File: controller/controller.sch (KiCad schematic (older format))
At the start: 23 parts, among them J1 PC104_40Pin_2.54mm, J2 Siren, U1 FM24W256-G, U2 SC16IS752IPW, U3 ADT7410TRZ, U4 MAX732MJA883B, X1 1.8432 MHz

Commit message: First commit: Proteus III PCB footprint
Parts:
- removed BT1: RN41, WhitworthStandard:xbee-standard, symbol WhitworthStandard:RN41
- removed C1: 22 pF, Capacitor_SMD:C_1206_3216Metric_Pad1.42x1.75mm_HandSolder, symbol Device:C
- removed C2: 33 pF, Capacitor_SMD:C_1206_3216Metric_Pad1.42x1.75mm_HandSolder, symbol Device:C
- removed R3: 1k, Resistor_SMD:R_1206_3216Metric_Pad1.42x1.75mm_HandSolder, symbol Device:R
- removed U2: SC16IS752IPW, SC16IS752:SC16IS752IPW, symbol SC16IS752IPW:SC16IS752IPW
- removed X1: 1.8432 MHz, Crystal:Crystal_HC49-U_Vertical, symbol Device:Crystal
- added XB1: XBee, WhitworthStandard:xbee-standard, symbol WhitworthStandard:XBee
- C3, C4, C5, C6, C7, C8: symbol Device:C -> controller-rescue:C-Device
- D1: symbol Device:D_Zener_ALT -> controller-rescue:D_Zener_ALT-Device
- J1: symbol controller-rescue:PC104_40Pin_2.54mm-WhitworthStandard -> controller-rescue:PC104_40Pin_2.54mm-WhitworthStandard-controller-rescue
- J2: symbol Connector:Screw_Terminal_01x02 -> controller-rescue:Screw_Terminal_01x02-Connector
- L1: symbol Device:L -> controller-rescue:L-Device
- MBED1: symbol WhitworthStandard:LPC1768 -> controller-rescue:LPC1768-WhitworthStandard
- R1, R2: symbol Device:R -> controller-rescue:R-Device
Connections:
- net labels added: Local_RX, Local_TX, Local_WAKE, USB_D+, USB_D-
- net labels removed: BT_RX, BT_TX, POD_RX, POD_TX, POD_WAKE, RADIO_RX, RADIO_TX, SERIAL_ALERT
- wire segments 65 -> 50
- no-connect marks 46 -> 30
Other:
- note removed: "I2C address set to 0x98\nA0 = VDD, V1 = GND"
- note removed: "Serial Multiplexer"

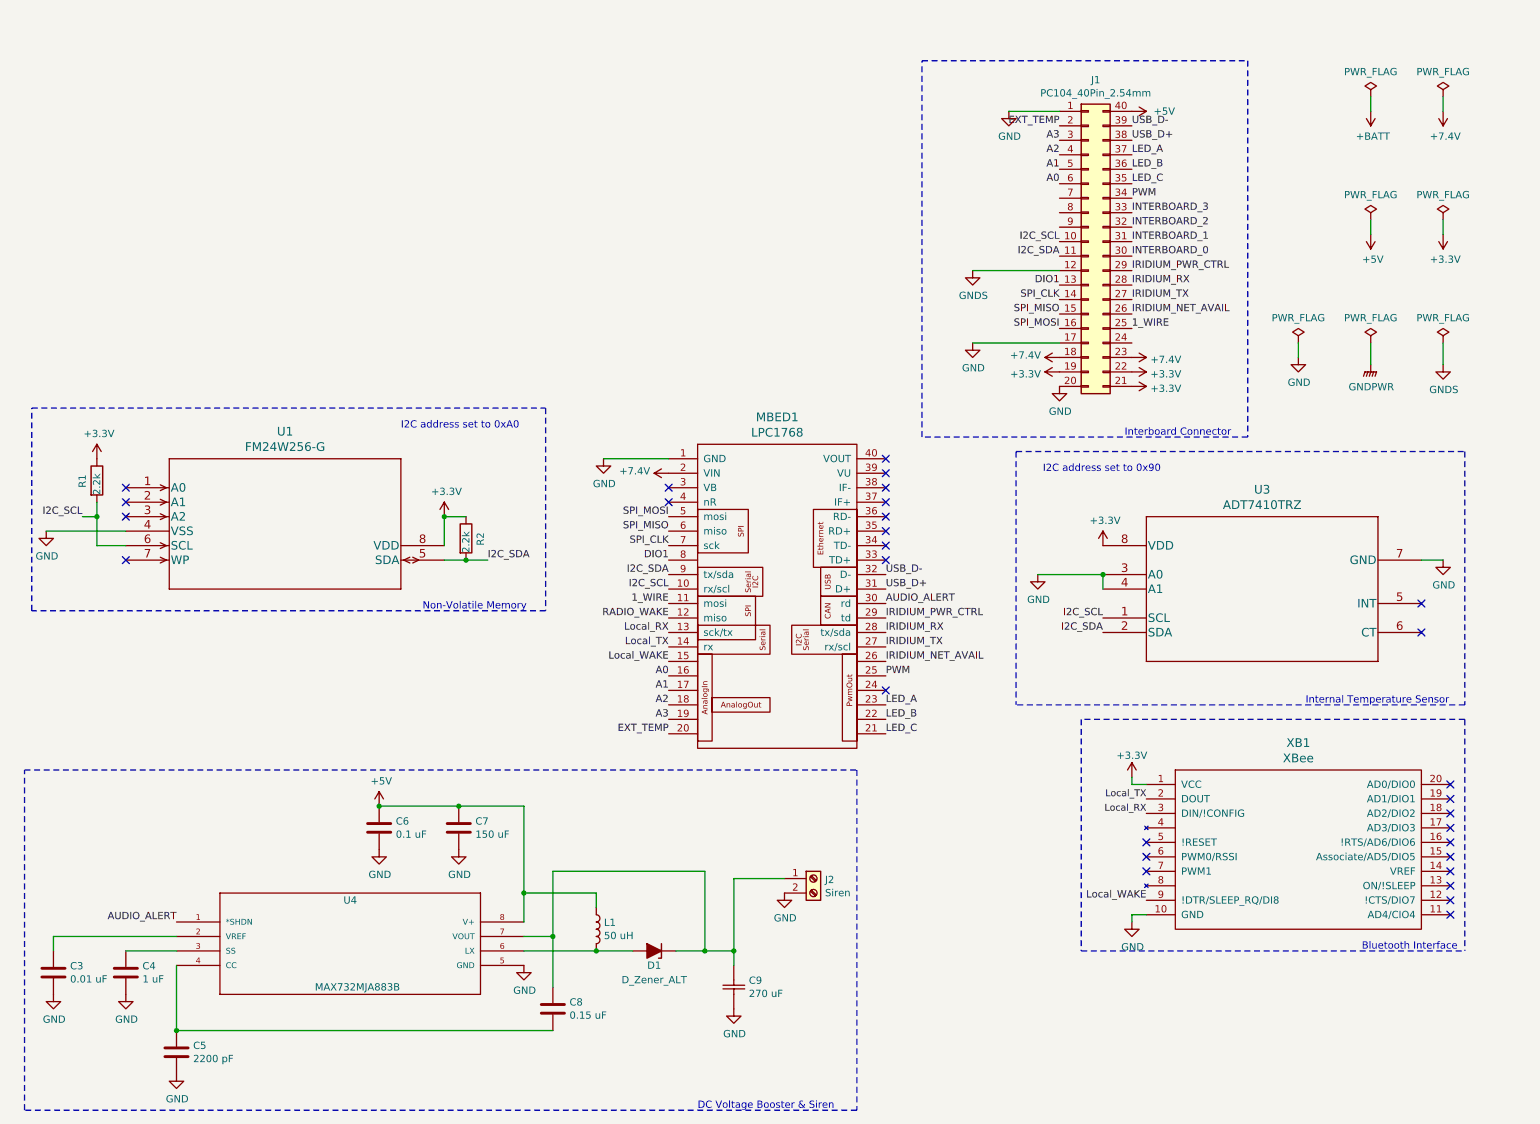
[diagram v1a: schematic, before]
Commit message: Updated controller board with proteus III and Zilog multiplexer
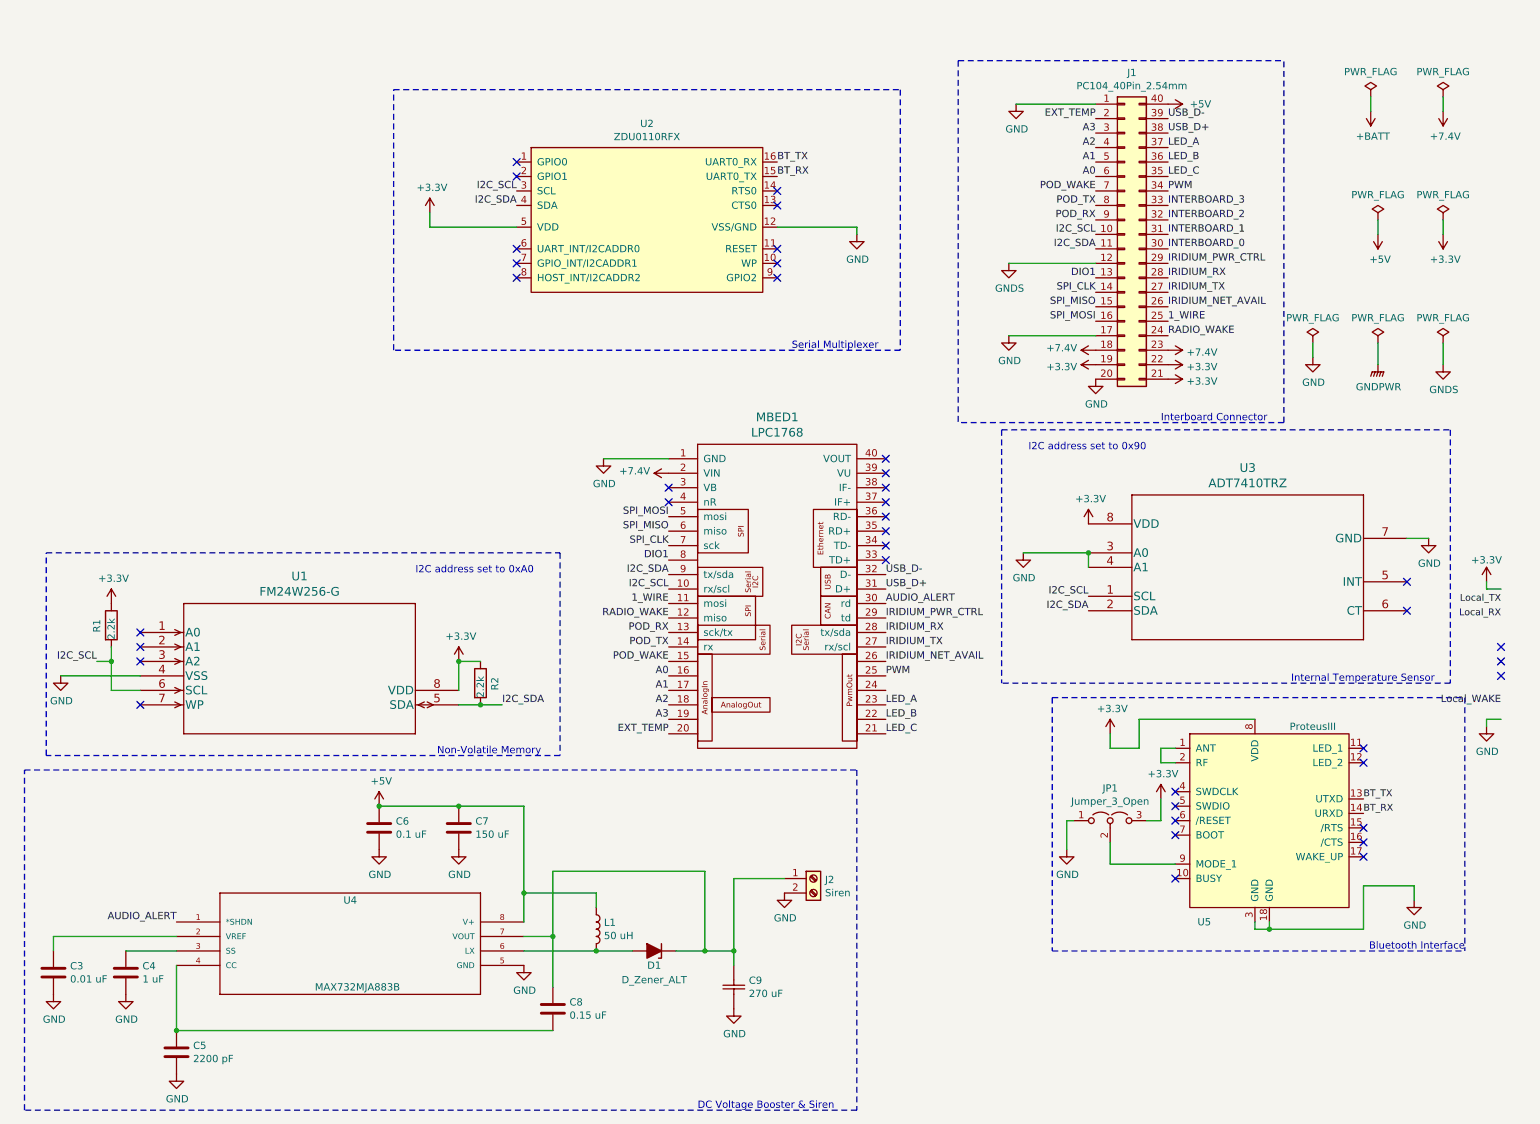
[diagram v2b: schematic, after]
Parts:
- removed XB1: XBee, WhitworthStandard:xbee-standard, symbol WhitworthStandard:XBee
- added JP1: Jumper_3_Open, Connector_PinHeader_2.54mm:PinHeader_1x03_P2.54mm_Vertical, symbol Jumper:Jumper_3_Open
- added U2: ZDU0110RFX, WhitworthStandard:ZDU0110RFX, symbol WhitworthStandard:ZDU0110RFX
- added U5: ProteusIII, WhitworthStandard:Proteus_III_hand_solder, symbol WhitworthStandard:ProteusIII
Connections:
- net +3V3: now also JP1.3 (B), U2.5 (VDD), U5.8 (VDD)
- net GND: now also JP1.1 (A), U2.12 (VSS/GND), U5.18 (GND), U5.3 (GND)
- net I2C_SCL: now also U2.3 (SCL)
- net I2C_SDA: now also U2.4 (SDA)
- net Local_RX: no longer MBED1.13 (sck/tx)
- net Local_TX: no longer MBED1.14 (rx)
- net Local_WAKE: no longer MBED1.15
- net RADIO_WAKE: now also J1.24 (Pin_24)
- net POD_WAKE: now reaches J1.7 (Pin_7)
- net POD_WAKE: now also MBED1.15
- net POD_TX: now reaches J1.8 (Pin_8)
- net POD_TX: now also MBED1.14 (rx)
- net POD_RX: now reaches J1.9 (Pin_9)
- net POD_RX: now also MBED1.13 (sck/tx)
- new net: U5.1 (ANT), U5.2 (RF)
- new net: JP1.2 (C), U5.9 (MODE_1)
- new net BT_RX: U2.15 (UART0_TX), U5.14 (URXD)
- new net BT_TX: U2.16 (UART0_RX), U5.13 (UTXD)
- no-connect marks 30 -> 39
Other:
- note added: "Serial Multiplexer"
- moved on the sheet: J1, R1, R2, U1, U3

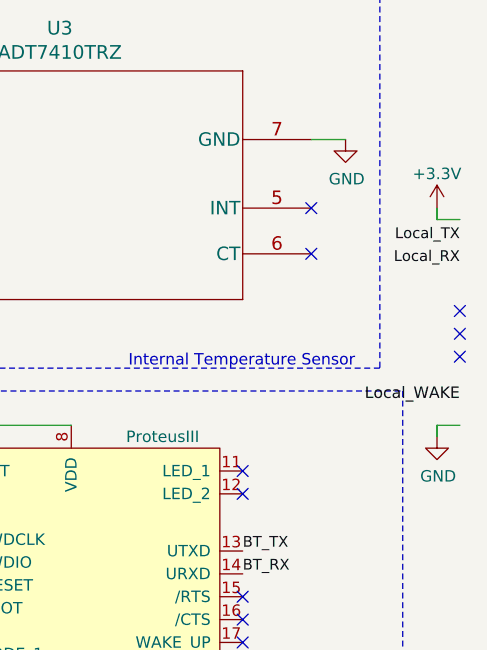
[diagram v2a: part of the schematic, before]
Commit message: 2nd commit mounting through holes added
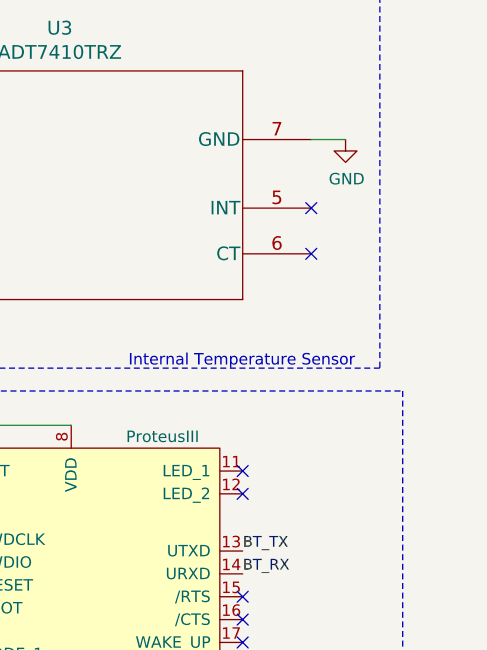
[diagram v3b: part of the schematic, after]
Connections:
- no-connect marks 39 -> 36
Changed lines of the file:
@@
 	0    -1   1    0
 $EndComp
-$Comp
-L power:+3.3V #PWR0125
-U 1 1 60EDA5DF
-P 10600 4150
-F 0 "#PWR0125" H 10600 4000 50  0001 C CNN
-F 1 "+3.3V" H 10600 4300 50  0000 C CNN
-F 2 "" H 10600 4150 50  0001 C CNN
-F 3 "" H 10600 4150 50  0001 C CNN
-	1    10600 4150
-	1    0    0    -1
-$EndComp
-Text Label 10700 4300 2    47   ~ 0
-Local_TX
-Text Label 10700 4400 2    47   ~ 0
-Local_RX
-Text Label 10700 5000 2    50   ~ 0
-Local_WAKE
-Wire Wire Line
-	10700 4200 10600 4200
-Wire Wire Line
-	10600 4200 10600 4150
-NoConn ~ 10700 4600
-NoConn ~ 10700 4700
-NoConn ~ 10700 4800
 Text Label 6450 4100 0    50   ~ 0
 USB_D-
@@
 Text Label 8400 1050 0    50   ~ 0
 USB_D+
-Wire Wire Line
-	10700 5100 10600 5100
-Wire Wire Line
-	10600 5100 10600 5150
-$Comp
-L power:GND #PWR0126
-U 1 1 60F3C4D1
-P 10600 5150
-F 0 "#PWR0126" H 10600 4900 50  0001 C CNN
-F 1 "GND" H 10605 4977 50  0000 C CNN
-F 2 "" H 10600 5150 50  0001 C CNN
-F 3 "" H 10600 5150 50  0001 C CNN
-	1    10600 5150
-	1    0    0    -1
-$EndComp
 Wire Notes Line
 	9200 3050 9200 550

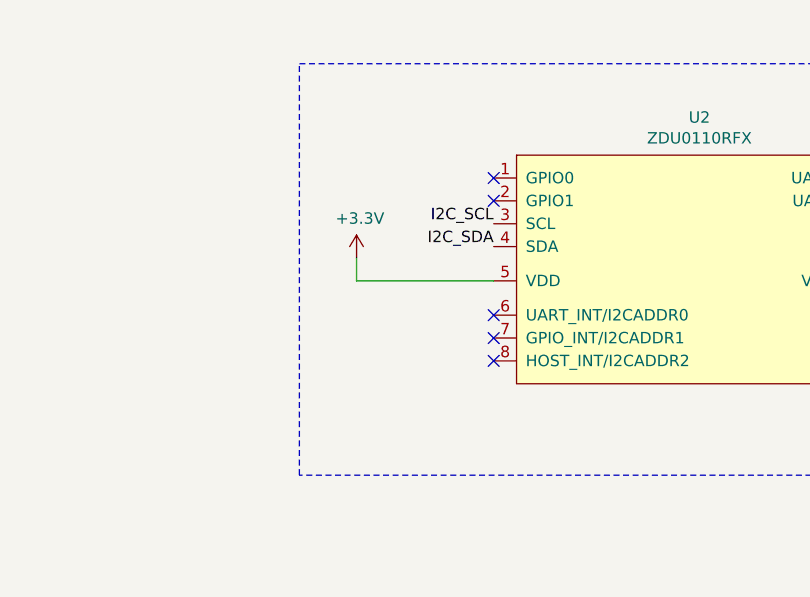
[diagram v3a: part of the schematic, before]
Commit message: ZDU0110RFX I2C address set
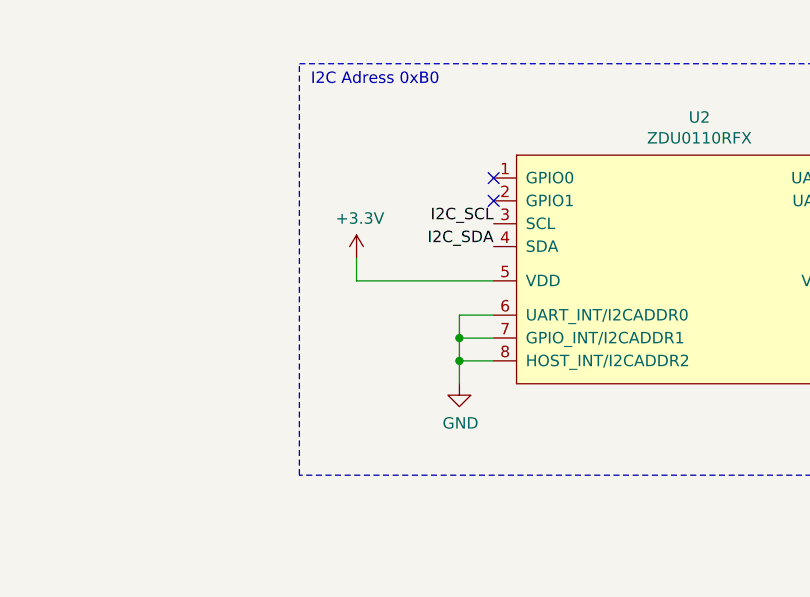
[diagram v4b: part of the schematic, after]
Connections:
- net GND: now also U2.6 (UART_INT/I2CADDR0), U2.7 (GPIO_INT/I2CADDR1), U2.8 (HOST_INT/I2CADDR2)
- no-connect marks 36 -> 33
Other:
- note added: "I2C Adress 0xB0"
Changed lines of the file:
@@
 NoConn ~ 3900 1250
 NoConn ~ 3900 1350
-NoConn ~ 3900 1850
-NoConn ~ 3900 1950
-NoConn ~ 3900 2050
 NoConn ~ 5700 2050
 NoConn ~ 5700 1950
@@
 Text Label 8400 2450 0    50   ~ 0
 RADIO_WAKE
+$Comp
+L power:GND #PWR0125
+U 1 1 60F2B4AC
+P 3750 2150
+F 0 "#PWR0125" H 3750 1900 50  0001 C CNN
+F 1 "GND" H 3755 1977 50  0000 C CNN
+F 2 "" H 3750 2150 50  0001 C CNN
+F 3 "" H 3750 2150 50  0001 C CNN
+	1    3750 2150
+	1    0    0    -1
+$EndComp
+Wire Wire Line
+	3900 1850 3750 1850
+Wire Wire Line
+	3750 1850 3750 1950
+Wire Wire Line
+	3900 1950 3750 1950
+Connection ~ 3750 1950
+Wire Wire Line
+	3750 1950 3750 2050
+Wire Wire Line
+	3900 2050 3750 2050
+Connection ~ 3750 2050
+Wire Wire Line
+	3750 2050 3750 2150
+Text Notes 3100 850  0    50   ~ 0
+I2C Adress 0xB0
 $EndSCHEMATC
